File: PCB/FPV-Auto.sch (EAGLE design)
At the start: 97 parts, among them Q310 CSD25402Q3A, Q320 BSS138, U100 ATMEGA328P-AU, U110 NRF24L01+_MINI, U120 74LVC2T45DCT, U140 DRV8835, U200 RASPBERRY_PI_ZERO_W_V1.1_GPIO, U210 MAX98357A, U300 BQ25892, U330 TPS61236P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

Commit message: Kommentare...
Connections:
- removed net STAT: R300.1, U300A.STAT
- new net N$20: LED300.A, LED301.A, R300.1
- net N$19: now also U300A.STAT; no longer R300.2
- net VBUS: now also R300.2; no longer LED300.A, LED301.A
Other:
- note added: "Hackffm-Mänchen in Stop-Lack"
- note added: "Poly GND für Audio Step-up Polygone"
- note added: "Version o. Datum auf PCB"
- note removed: "680pF(eval-board) vs 220pF(Adafruit-board)"
- note removed: "Yes please, this is better for antenna"
- note removed: "Z-Diode mit 8-10V im SC79 bzw SOT523 package nehmen, z.B. https://www.mouser.de/datasheet/2/348/edzvfht2r9.1b-e-1493803.pdf Kondensator am Gate halte ich für Unsinn."
- note removed: "changed pin"
- note removed: "changed pin again, double check all"
- note removed: "done"
- note removed: "pin 9 connected to GND add polygon"
- note removed: "stand so in deiner Vorlage"
- moved on the sheet: LED300, LED301, R300
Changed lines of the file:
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@@
 12dB 1-C   0R
 15dB 1-C 100K</text>
-<text x="292.1" y="35.56" size="1.778" layer="150" rot="R90">680pF(eval-board) vs 220pF(Adafruit-board)</text>
 <text x="48.26" y="116.84" size="6.35" layer="94" rot="R180" align="bottom-center">ISP</text>
 <text x="226.06" y="116.84" size="6.35" layer="94" rot="R180" align="bottom-center">I2S Audio Amplifier</text>
@@
 <text x="96.52" y="58.42" size="1.778" layer="97" align="bottom-center">button
 connector</text>
-<text x="91.44" y="17.78" size="1.778" layer="150" align="center">RASPI GPIO #22</text>
+<text x="91.44" y="15.24" size="1.778" layer="150" align="center">RASPI GPIO #22</text>
 <text x="121.92" y="116.84" size="6.35" layer="94" rot="R180" align="bottom-center">Power on and
 programming
@@
 <text x="203.2" y="20.32" size="1.27" layer="97" align="top-left">R211 = default open
 (should be good for Raspberry)</text>
-<text x="337.82" y="198.12" size="1.778" layer="254">Yes please, this is
-better for antenna </text>
 <text x="195.58" y="154.94" size="1.4224" layer="97" rot="R90">Arduino avrdude w auto-reset:
 https://github.com/SpellFoundry/avrdude-rpi</text>
-<text x="305.816" y="205.994" size="1.778" layer="150" align="center-left">pin 9 connected to GND
-add polygon</text>
 <text x="340.36" y="27.94" size="1.4224" layer="94">Unsere Namen hier irgendwo</text>
 <text x="172.72" y="137.16" size="1.4224" layer="254" rot="R90">All pins checked -  seems to be ok.</text>
@@
 matter - all supplies held
 by button already.</text>
-<text x="147.32" y="38.1" size="1.4224" layer="254">Add-on to detect
+<text x="142.24" y="35.56" size="1.4224" layer="254">Add-on to detect
 button press after start-up</text>
-<text x="154.94" y="198.12" size="1.778" layer="150" align="center-left">changed pin again, double check all</text>
-<text x="154.94" y="195.58" size="1.778" layer="150" align="center-left">changed pin again, double check all</text>
-<text x="154.94" y="193.04" size="1.778" layer="150" align="center-left">changed pin again, double check all</text>
-<text x="154.94" y="190.5" size="1.778" layer="150" align="center-left">changed pin again, double check all</text>
-<text x="154.94" y="139.7" size="1.778" layer="150" align="center-left">changed pin again, double check all</text>
-<text x="154.94" y="180.34" size="1.778" layer="150" align="center-left">changed pin</text>
 </plain>
 <instances>
@@
 <text x="129.54" y="177.8" size="1.778" layer="150" align="center">AGND</text>
 <text x="91.44" y="119.38" size="1.778" layer="94">Max. 14V</text>
-<text x="170.18" y="38.1" size="1.778" layer="94">Z-Diode mit 8-10V im SC79 bzw SOT523 package nehmen, z.B.
-https://www.mouser.de/datasheet/2/348/edzvfht2r9.1b-e-1493803.pdf
-Kondensator am Gate halte ich für Unsinn.</text>
-<text x="175.26" y="50.8" size="1.778" layer="150" align="center">done</text>
-<text x="190.5" y="35.56" size="1.778" layer="150" align="center">stand so in deiner Vorlage</text>
+<text x="193.04" y="215.9" size="1.778" layer="254">Poly GND für Audio
+Step-up Polygone</text>
+<text x="185.42" y="210.82" size="1.778" layer="254">Version o. Datum auf PCB</text>
+<text x="180.34" y="208.28" size="1.778" layer="254">Hackffm-Mänchen in Stop-Lack</text>
 </plain>
 <instances>
@@
 <instance part="C300" gate="A" x="40.64" y="180.34" rot="R90"/>
 <instance part="GND15" gate="1" x="40.64" y="160.02"/>
-<instance part="R300" gate="A" x="66.04" y="193.04" rot="MR0"/>
+<instance part="R300" gate="A" x="50.8" y="193.04" rot="MR0"/>
 <instance part="R333" gate="A" x="259.08" y="185.42"/>
 <instance part="R334" gate="A" x="259.08" y="175.26"/>
@@
 </instance>
 <instance part="+3V8" gate="G$1" x="370.84" y="63.5" rot="MR0"/>
-<instance part="LED300" gate="G$1" x="50.8" y="193.04" rot="MR270"/>
+<instance part="LED300" gate="G$1" x="63.5" y="195.58" rot="MR270"/>
 <instance part="PAD_BAT+" gate="G$1" x="144.78" y="124.46" smashed="yes" rot="MR0">
 <attribute name="NAME" x="147.32" y="124.46" size="1.778" layer="95" align="center-left"/>
@@
 </instance>
 <instance part="GND31" gate="1" x="48.26" y="33.02"/>
-<instance part="LED301" gate="G$1" x="50.8" y="187.96" rot="MR270"/>
+<instance part="LED301" gate="G$1" x="63.5" y="190.5" rot="MR270"/>
 <instance part="GND32" gate="1" x="289.56" y="172.72"/>
 <instance part="GND33" gate="1" x="335.28" y="180.34"/>
@@
 <segment>
 <pinref part="U300" gate="A" pin="VBUS"/>
-<wire x1="73.66" y1="198.12" x2="45.72" y2="198.12" width="0.1524" layer="91"/>
-<label x="43.18" y="198.12" size="1.778" layer="95" rot="R180" xref="yes"/>
-<wire x1="45.72" y1="198.12" x2="43.18" y2="198.12" width="0.1524" layer="91"/>
-<wire x1="48.26" y1="193.04" x2="45.72" y2="193.04" width="0.1524" layer="91"/>
-<wire x1="45.72" y1="198.12" x2="45.72" y2="193.04" width="0.1524" layer="91"/>
-<junction x="45.72" y="198.12"/>
-<pinref part="LED300" gate="G$1" pin="A"/>
-<pinref part="LED301" gate="G$1" pin="A"/>
-<wire x1="45.72" y1="193.04" x2="45.72" y2="187.96" width="0.1524" layer="91"/>
-<wire x1="45.72" y1="187.96" x2="48.26" y2="187.96" width="0.1524" layer="91"/>
-<junction x="45.72" y="193.04"/>
+<wire x1="73.66" y1="198.12" x2="40.64" y2="198.12" width="0.1524" layer="91"/>
+<label x="35.56" y="198.12" size="1.778" layer="95" rot="R180" xref="yes"/>
+<wire x1="40.64" y1="198.12" x2="35.56" y2="198.12" width="0.1524" layer="91"/>
+<wire x1="40.64" y1="198.12" x2="40.64" y2="193.04" width="0.1524" layer="91"/>
+<junction x="40.64" y="198.12"/>
+<pinref part="R300" gate="A" pin="2"/>
+<wire x1="40.64" y1="193.04" x2="45.72" y2="193.04" width="0.1524" layer="91"/>
 </segment>
 <segment>
@@
 </segment>
 </net>
-<net name="STAT" class="0">
-<segment>
-<pinref part="U300" gate="A" pin="STAT"/>
-<pinref part="R300" gate="A" pin="1"/>
-<wire x1="73.66" y1="193.04" x2="71.12" y2="193.04" width="0.1524" layer="91"/>
-</segment>
-</net>
 <net name="N$19" class="0">
 <segment>
-<pinref part="R300" gate="A" pin="2"/>
-<wire x1="55.88" y1="193.04" x2="58.42" y2="193.04" width="0.1524" layer="91"/>
+<wire x1="68.58" y1="195.58" x2="71.12" y2="195.58" width="0.1524" layer="91"/>
 <pinref part="LED300" gate="G$1" pin="C"/>
 <pinref part="LED301" gate="G$1" pin="C"/>
-<wire x1="58.42" y1="193.04" x2="60.96" y2="193.04" width="0.1524" layer="91"/>
-<wire x1="55.88" y1="187.96" x2="58.42" y2="187.96" width="0.1524" layer="91"/>
-<wire x1="58.42" y1="187.96" x2="58.42" y2="193.04" width="0.1524" layer="91"/>
-<junction x="58.42" y="193.04"/>
+<wire x1="68.58" y1="190.5" x2="71.12" y2="190.5" width="0.1524" layer="91"/>
+<wire x1="71.12" y1="190.5" x2="71.12" y2="193.04" width="0.1524" layer="91"/>
+<pinref part="U300" gate="A" pin="STAT"/>
+<wire x1="71.12" y1="193.04" x2="71.12" y2="195.58" width="0.1524" layer="91"/>
+<wire x1="71.12" y1="193.04" x2="73.66" y2="193.04" width="0.1524" layer="91"/>
+<junction x="71.12" y="193.04"/>
 </segment>
 </net>
@@
 </segment>
 </net>
+<net name="N$20" class="0">
+<segment>
+<pinref part="LED301" gate="G$1" pin="A"/>
+<pinref part="LED300" gate="G$1" pin="A"/>
+<wire x1="60.96" y1="195.58" x2="58.42" y2="195.58" width="0.1524" layer="91"/>
+<wire x1="58.42" y1="195.58" x2="58.42" y2="193.04" width="0.1524" layer="91"/>
+<wire x1="58.42" y1="193.04" x2="58.42" y2="190.5" width="0.1524" layer="91"/>
+<wire x1="58.42" y1="190.5" x2="60.96" y2="190.5" width="0.1524" layer="91"/>
+<pinref part="R300" gate="A" pin="1"/>
+<wire x1="55.88" y1="193.04" x2="58.42" y2="193.04" width="0.1524" layer="91"/>
+<junction x="58.42" y="193.04"/>
+</segment>
+</net>

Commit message: Updated PCB
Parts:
- U200: value RASPBERRY_PI_ZERO_W_V1.1_GPIO -> RASPBERRY_PI_ZERO_W_V1.1_GPIO_DUAL; device FPV-Auto:RASPBERRY_PI_ZERO_W_V1.1_GPIO -> FPV-Auto:RASPBERRY_PI_ZERO_W_V1.1_GPIO_DUAL
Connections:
- removed net NRF_CE: U100A.PC3, U110.CE
- removed net NRF_MOSI: U100A.PC0, U110.MOSI
- removed net SCK/NRF_MISO: U100A.PB5, U110.MISO, X100.SCK
- new net NRF_CS: U100A.PC0, U110.CE
- new net NRF_MISO: U100A.PC3, U110.MISO
- new net SCK/NRF_MOSI: U100A.PB5, U110.MOSI, X100.SCK
- net N$15: now also D320.K2; no longer D320.K1
- net N$18: now also D320.K1; no longer D320.K2
- net NRF_!CS: now also U100A.PC1; no longer U100A.PC2
- net NRF_SCK: now also U100A.PC2; no longer U100A.PC1
- net VO+: now also X210.1; no longer X210.2
- net VO-: now also X210.2; no longer X210.1
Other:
- moved on the sheet: D320, R200, R201, X210

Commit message: Board Layout Update
changed mask, changed 0402 caps -> 0603
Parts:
- C331, C341: device FPV-Auto:C0402 -> FPV-Auto:C0603
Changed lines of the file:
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@@
 <part name="R332" library="FPV-Auto" deviceset="R" device="" value="324K"/>
 <part name="R330" library="FPV-Auto" deviceset="R" device="" value="1M"/>
-<part name="C331" library="FPV-Auto" deviceset="C" device="0402" value="1µF"/>
+<part name="C331" library="FPV-Auto" deviceset="C" device="0603" value="1µF"/>
 <part name="C330" library="FPV-Auto" deviceset="C" device="0603" value="10µF"/>
 <part name="C332" library="FPV-Auto" deviceset="C" device="0805" value="22µF"/>
@@
 <part name="R342" library="FPV-Auto" deviceset="R" device="" value="294K"/>
 <part name="R340" library="FPV-Auto" deviceset="R" device="" value="1M"/>
-<part name="C341" library="FPV-Auto" deviceset="C" device="0402" value="1µF"/>
+<part name="C341" library="FPV-Auto" deviceset="C" device="0603" value="1µF"/>
 <part name="C340" library="FPV-Auto" deviceset="C" device="0603" value="10µF"/>
 <part name="C342" library="FPV-Auto" deviceset="C" device="0805" value="22µF"/>

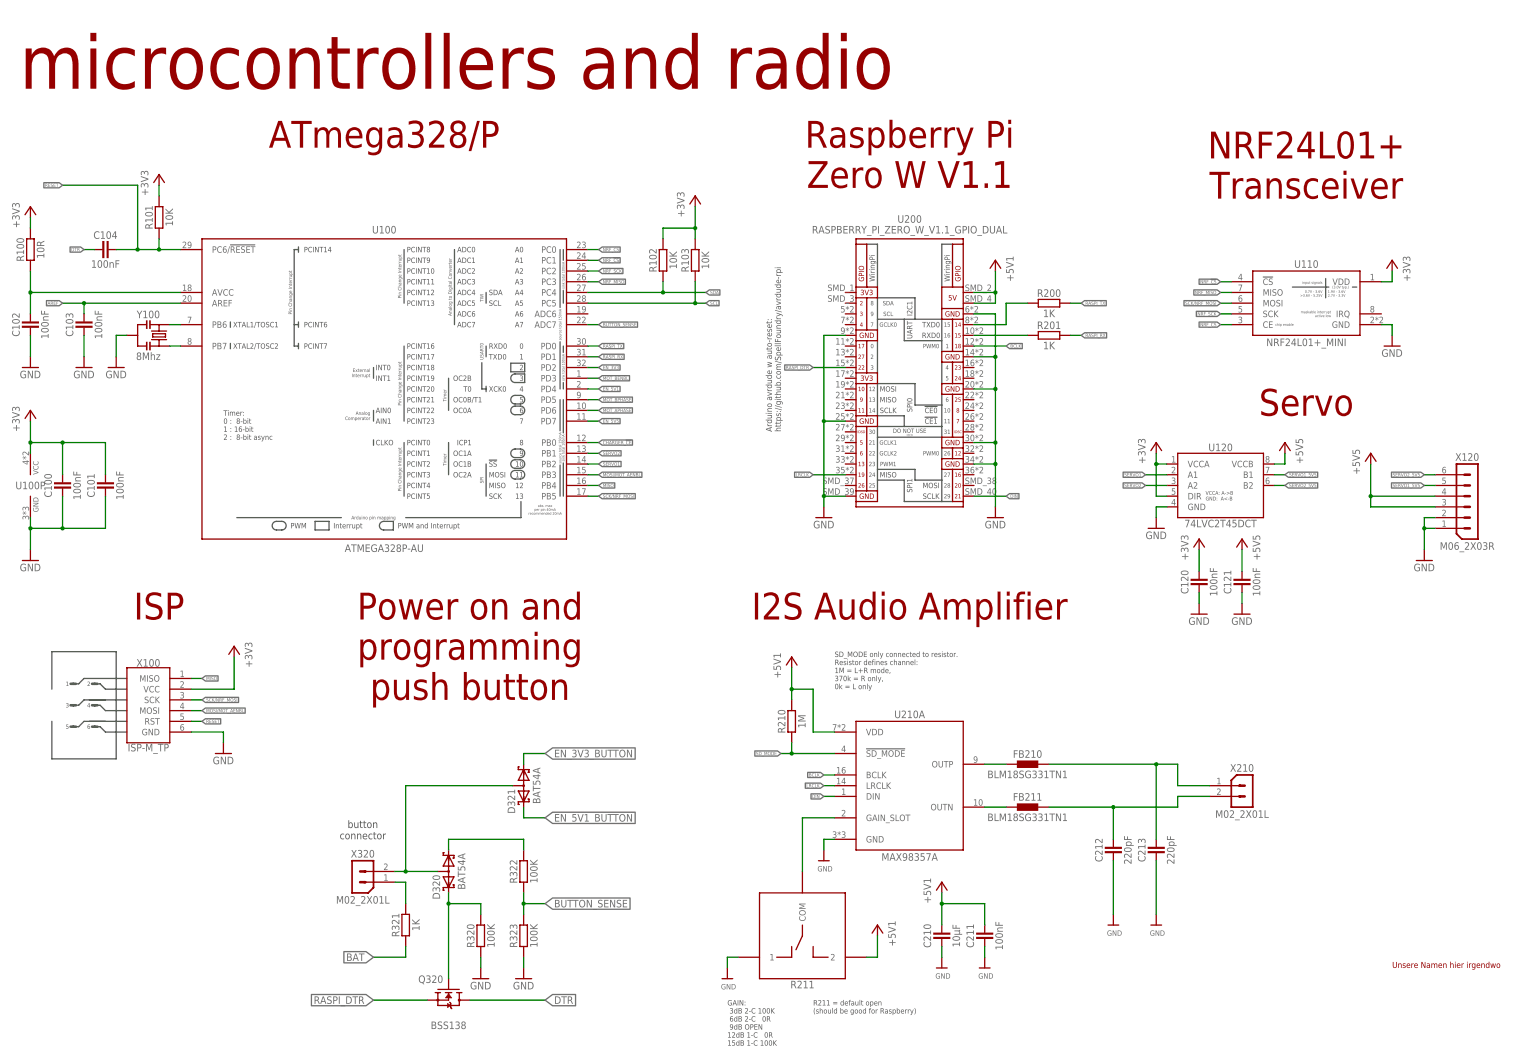
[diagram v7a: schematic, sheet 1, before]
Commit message: Silkscreen and Schematic Docu updates
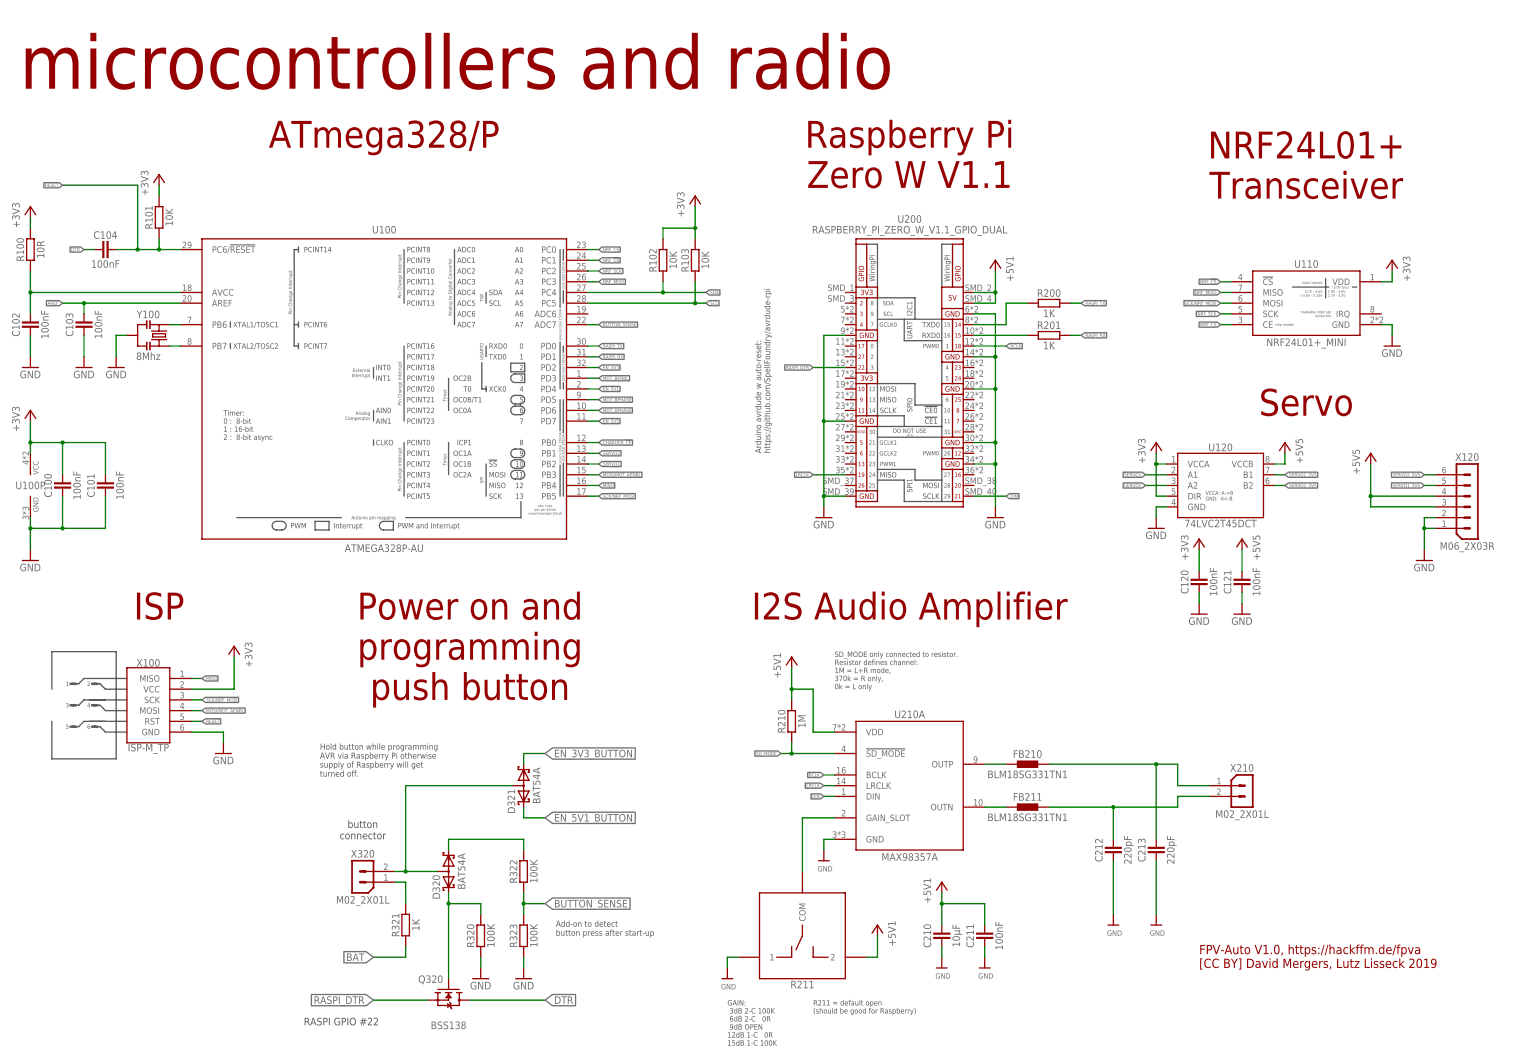
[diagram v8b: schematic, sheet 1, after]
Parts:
- RT301: value (none) -> NTCS0603E3103FLT
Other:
- note added: "FPV-Auto V1.0, https://hackffm.de/fpva [CC BY] David Mergers, Lutz Lisseck 2019"
- note added: "Hold button while programming AVR via Raspberry Pi otherwise supply of Raspberry will get turned off."
- note removed: "All pins checked - seems to be ok."
- note removed: "DIN, BCLK, LRCLK was on wrong pins (was pin# instead GPIO#). Should be now: DIN=GPIO21, BLCK=GPIO18, LRCLK=GPIO19"
- note removed: "Hackffm-Mänchen in Stop-Lack"
- note removed: "Poly GND für Audio Step-up Polygone"
- note removed: "Reset on power-up does not matter - all supplies held by button already."
- note removed: "Unsere Namen hier irgendwo"
- note removed: "Version o. Datum auf PCB"
- note removed: "changed L please verify"
- note removed: "choose SMD NTC"
- note removed: "test circuit!!! we might reset arduino on powerup"
